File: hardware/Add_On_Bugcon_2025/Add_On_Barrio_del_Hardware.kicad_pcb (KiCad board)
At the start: 2 copper layers, 25.7 x 48.3 mm, 21 parts, among them Q1 2N7002, Q2 2N7002, SW1 SW_RST, SW2 On

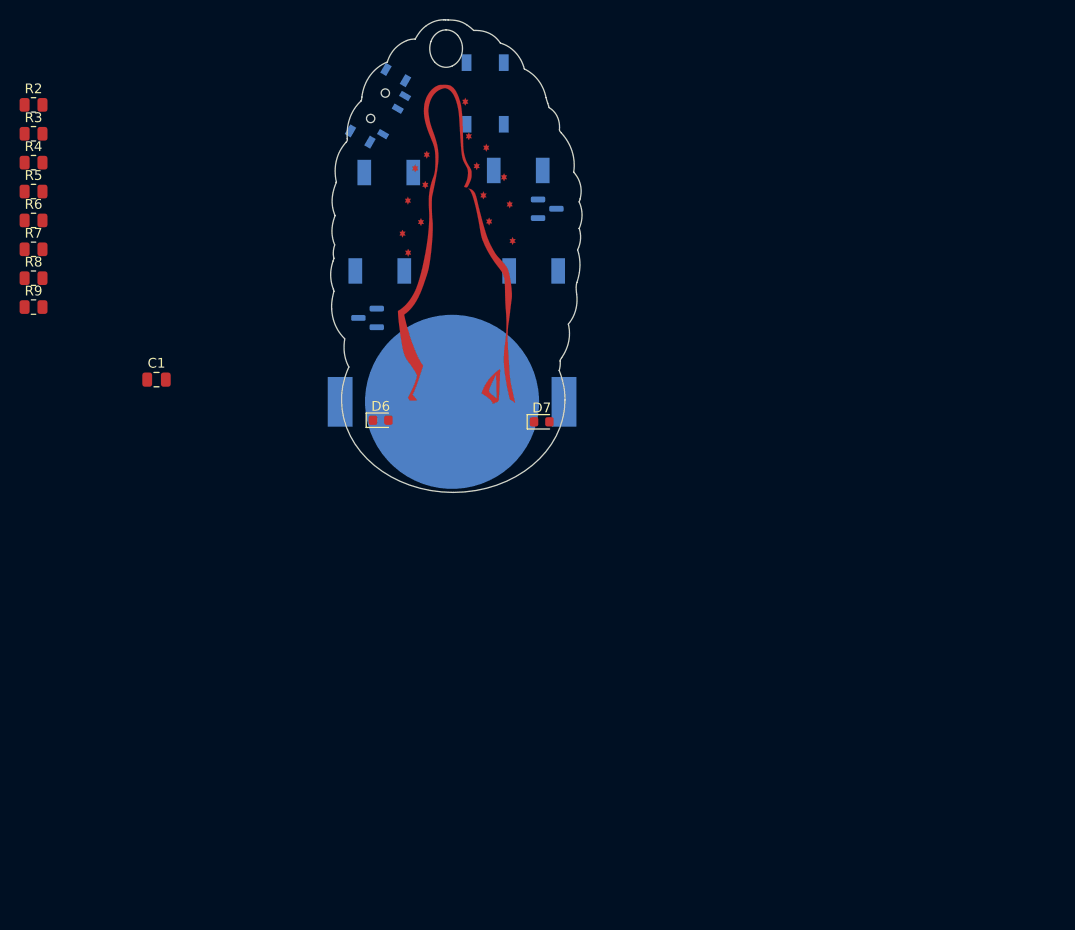
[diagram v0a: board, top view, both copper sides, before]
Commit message: feat(Hw):Update_And_Route_PCB
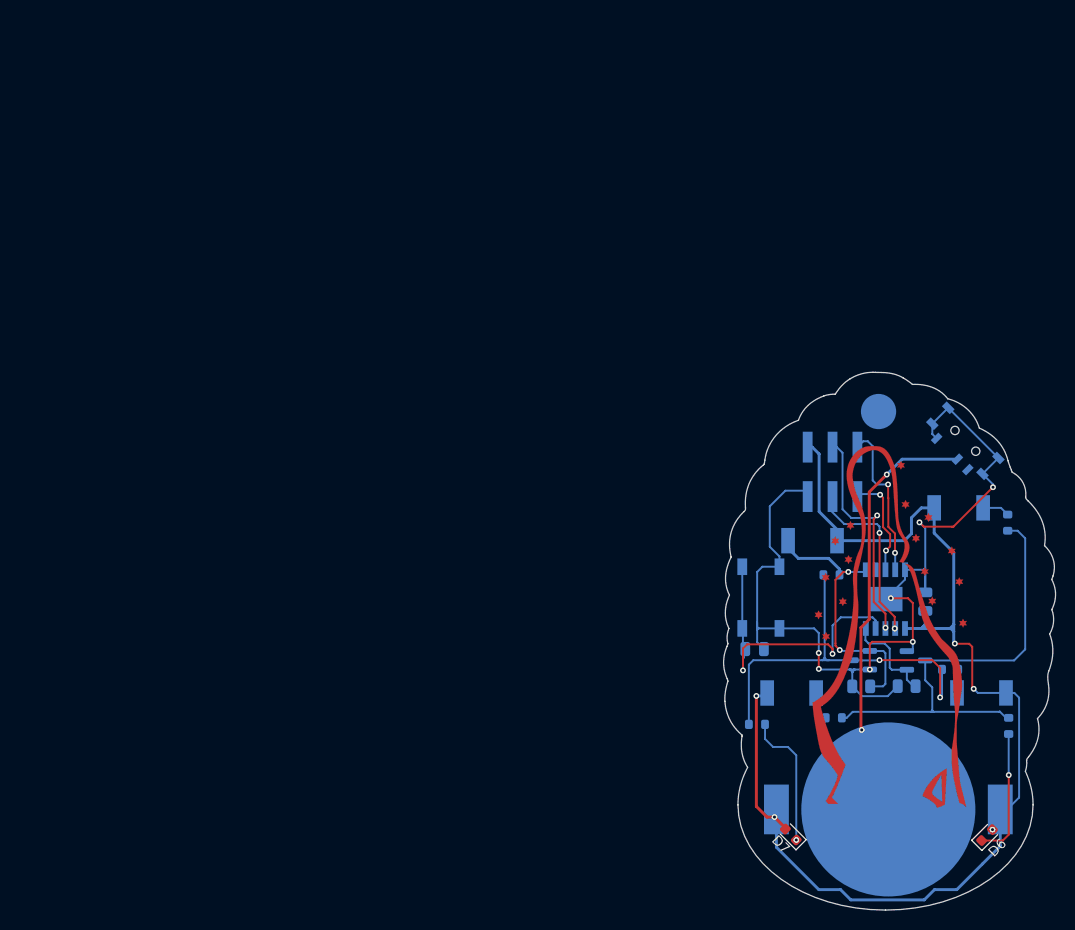
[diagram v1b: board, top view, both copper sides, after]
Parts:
- added C2: 0.1uF, Capacitor_SMD:C_0805_2012Metric, B.Cu at (131.1, 82.0)
- added J2: Conn_02x03_Odd_Even, Connector_PinHeader_2.54mm:PinHeader_2x03_P2.54mm_Vertical_SMD, B.Cu at (139.1, 63.9)
- added REF**: MountingHole_2.2mm_M2, MountingHole:MountingHole_2.2mm_M2, B.Cu at (143.8, 57.8)
- added U1: PY32F002AA15M6TU, Add_on:PY32F002AA15M, B.Cu at (144.5, 76.9)
- C1, R6, R7: moved to B.Cu
- R2, R3, R4, R5, R8, R9: value 180R -> 330R; footprint Resistor_SMD:R_0805_2012Metric -> Resistor_SMD:R_0603_1608Metric; moved to B.Cu
- moved R8 109.6 mm to (157.1, 89.9), turned to -90 degrees
- moved R2 108.3 mm to (157.0, 69.1), turned to 90 degrees
- moved R4 107.0 mm to (151.1, 84.1)
- moved R3 101.2 mm to (139.2, 89.0), turned to 180 degrees
- moved R6 101.1 mm to (146.7, 85.8), turned to 180 degrees
- moved R7 95.6 mm to (142.0, 85.8), turned to 180 degrees
- moved R5 90.4 mm to (139.0, 74.4)
- moved R9 85.3 mm to (131.4, 89.7)
- moved C1 81.7 mm to (148.6, 77.2), turned to 90 degrees
- moved D6 75.0 mm to (154.9, 101.0), turned to 45 degrees
- moved SW2 69.1 mm to (152.7, 60.7), turned to -45 degrees
- moved D2 67.5 mm to (152.0, 67.6)
- moved D4 62.8 mm to (154.3, 86.5), turned to 0 degrees
- moved Q2 61.3 mm to (142.0, 83.2)
- moved BT1 61.0 mm to (144.8, 98.4)
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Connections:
- Q1 pad 1: /PA3 -> /PA1
- Q2 pad 1: /PA1 -> /PA6
- R6 pad 1: /PA3 -> /PA1
- R7 pad 1: /PA1 -> /PA6
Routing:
- net +3.3V: track 0.00 -> 126.6 mm, vias 0 -> 5
- net GND: track 0.00 -> 102.1 mm, vias 0 -> 7
- net Net-(Q1-D): track 0.00 -> 47.5 mm
- net Net-(BT1--): track 0.00 -> 44.3 mm, vias 0 -> 2
- net Net-(Q2-D): track 0.00 -> 41.5 mm, vias 0 -> 2
- net /NRST: track 0.00 -> 31.7 mm, vias 0 -> 2
- net /TX: track 0.00 -> 23.2 mm, vias 0 -> 2
- net /PA6: track 0.00 -> 20.5 mm, vias 0 -> 2
- net /RX: track 0.00 -> 18.2 mm, vias 0 -> 2
- net /SWCLK: track 0.00 -> 16.3 mm, vias 0 -> 2
- net Net-(D7-K): track 0.00 -> 14.0 mm, vias 0 -> 1
- net Net-(D6-K): track 0.00 -> 13.3 mm, vias 0 -> 1
- net /SWDIO: track 0.00 -> 10.8 mm, vias 0 -> 2
- net /PA1: track 0.00 -> 10.0 mm
- net Net-(D5-K): track 0.00 -> 7.48 mm
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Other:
- board size 25.7 x 48.3 mm -> 33.9 x 54.9 mm

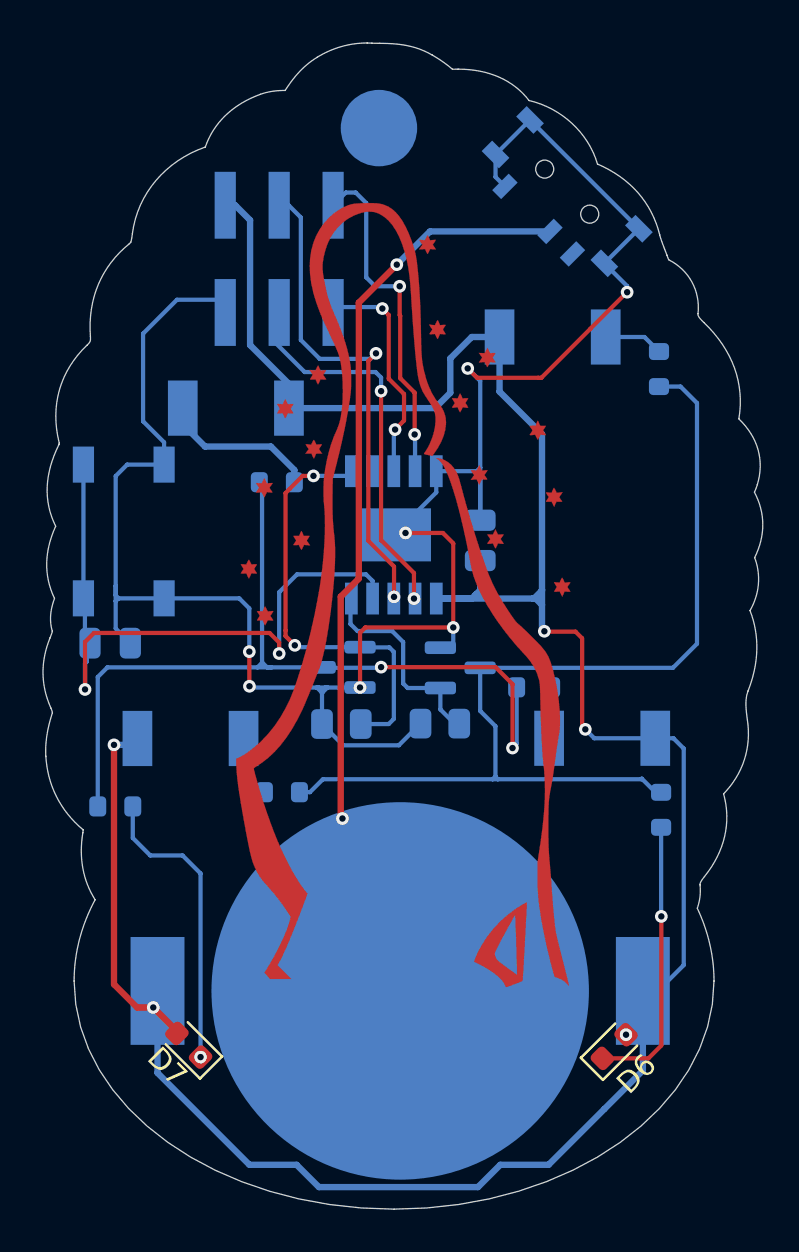
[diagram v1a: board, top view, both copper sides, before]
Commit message: feat(Hw)_Update PCB_Hole_Added
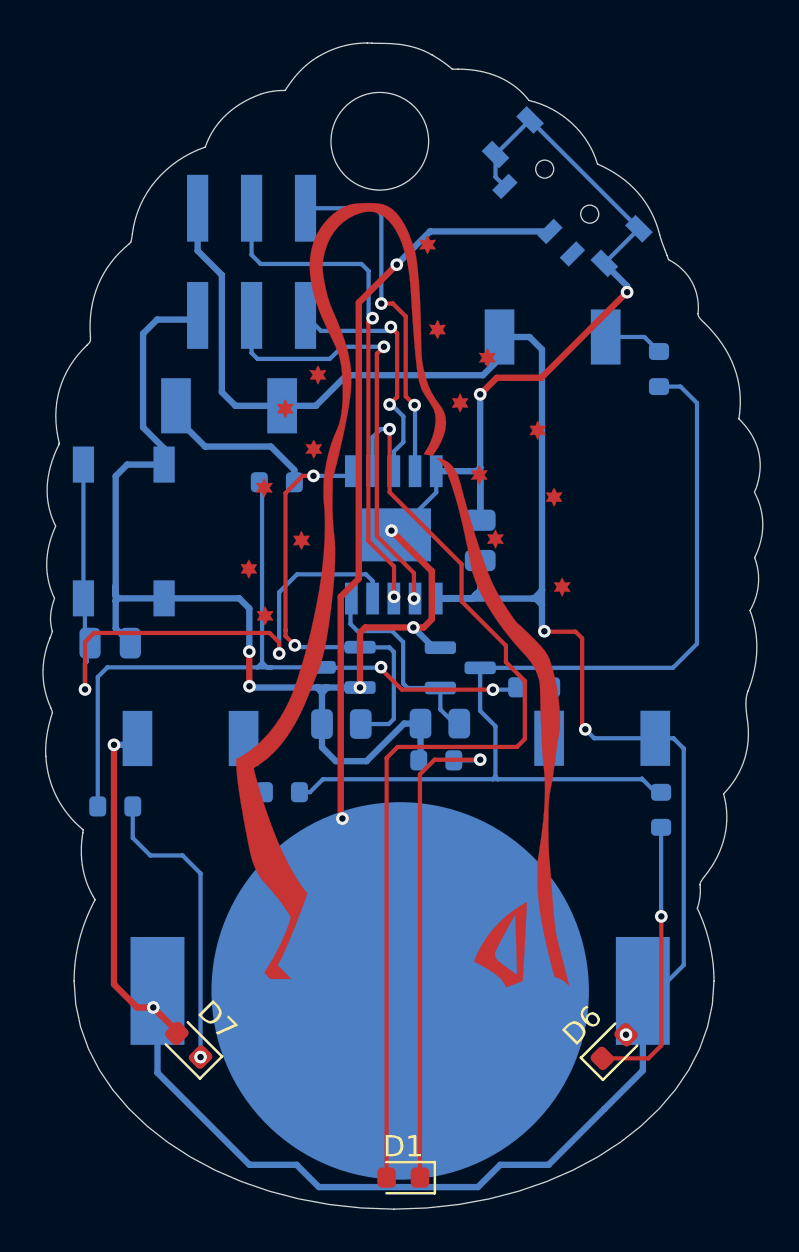
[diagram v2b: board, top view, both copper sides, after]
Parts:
- removed REF**: MountingHole_2.2mm_M2, MountingHole:MountingHole_2.2mm_M2
- added D1: White, LED_SMD:LED_0603_1608Metric, F.Cu at (144.9, 107.2)
- added R1: 330R, Resistor_SMD:R_0603_1608Metric, B.Cu at (146.5, 87.5)
- added kibuzzard-68DB0924: G***, kibuzzard-68DB0924, B.Cu at (148.5, 56.8)
- added kibuzzard-68DB0A49: G***, kibuzzard-68DB0A49, B.Cu at (133.8, 67.6)
- added kibuzzard-68DB0A69: G***, kibuzzard-68DB0A69, B.Cu at (133.8, 60.8)
- added kibuzzard-68DB0B59: G***, kibuzzard-68DB0B59, B.Cu at (137.8, 58.8)
- added kibuzzard-68DB0B66: G***, kibuzzard-68DB0B66, B.Cu at (142.2, 67.6)
- added kibuzzard-68DB0B8C: G***, kibuzzard-68DB0B8C, B.Cu at (135.5, 76.7)
- D6: value Pink -> Red
- D7: value Pink -> Green
- moved J2 1.31 mm to (137.8, 64.0)
- moved D5 0.34 mm to (136.7, 70.8)
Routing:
- net /PA7: track 0.00 -> 46.4 mm, vias 0 -> 1
- net Net-(D1-K): track 0.00 -> 23.4 mm, vias 0 -> 1
- net Net-(Q2-D): track 41.5 -> 36.0 mm
- net GND: track 102.1 -> 99.0 mm
- net /RX: track 18.2 -> 21.1 mm
- net +3.3V: track 126.6 -> 128.5 mm
- net /SWDIO: track 10.8 -> 12.2 mm
- net /TX: track 23.2 -> 24.1 mm
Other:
- outline, holes or cut-outs redrawn

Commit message: feat(Hw):Update_PCB_Added_Bac_Image
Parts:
- removed kibuzzard-68DB0A49: G***, kibuzzard-68DB0A49
- removed kibuzzard-68DB0A69: G***, kibuzzard-68DB0A69
- removed kibuzzard-68DB0B59: G***, kibuzzard-68DB0B59
- removed kibuzzard-68DB0B66: G***, kibuzzard-68DB0B66
- removed kibuzzard-68DB0B8C: G***, kibuzzard-68DB0B8C
